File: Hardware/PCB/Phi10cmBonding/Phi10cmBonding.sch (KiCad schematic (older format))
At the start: 2 parts

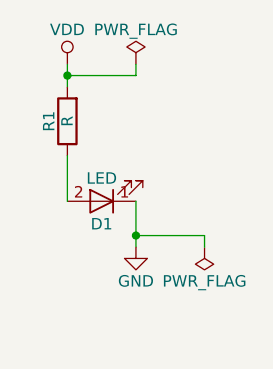
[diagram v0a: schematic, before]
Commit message: First example of correct net handling and zone filling
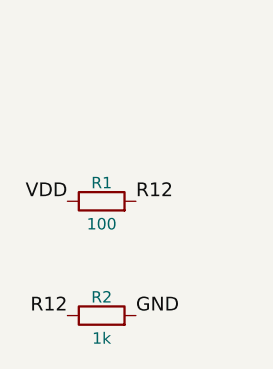
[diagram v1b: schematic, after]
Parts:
- removed D1: LED, LEDs:LED_0603, symbol LED
- added R2: 1k, Resistors_SMD:R_0603_HandSoldering, symbol R
- R1: value R -> 100
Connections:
- net GND: now also R2.2
- net VDD: now also R1.1; no longer R1.2
- new net R12: R1.2, R2.1
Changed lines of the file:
@@
 encoding utf-8
 Sheet 1 1
-Title "Topmetal-S sensor tiled plane, 10cm diameter version"
-Date "2017-03-28"
+Title "Python generated schematic with two resistors"
+Date ""
 Rev "0"
-Comp "LBNL"
+Comp "KiSch"
 Comment1 ""
 Comment2 ""
@@
 $EndDescr
 $Comp
-L LED D1
-U 1 1 58DA1C98
+L R R1
+U 1 1 58E4B144
 P 8000 5000
-F 0 "D1" H 8000 5100 50  0000 C CNN
-F 1 "LED" H 8000 4900 50  0000 C CNN
-F 2 "LEDs:LED_0603" H 8000 5000 50  0001 C CNN
+F 0 "R1" V 8080 5000 50  0000 C CNN
+F 1 "100" V 7900 5000 50  0000 C CNN
+F 2 "Resistors_SMD:R_0603_HandSoldering" V 7930 5000 50  0001 C CNN
 F 3 "" H 8000 5000 50  0001 C CNN
-	1    8000 5000
-	-1   0    0    1
+        1    8000 5000
+        0    -1   -1   0
 $EndComp
 $Comp
-L GND #PWR01
-U 1 1 58DA1D97
-P 8150 5200
-F 0 "#PWR01" H 8150 4950 50  0001 C CNN
-F 1 "GND" H 8150 5050 50  0000 C CNN
-F 2 "" H 8150 5200 50  0001 C CNN
-F 3 "" H 8150 5200 50  0001 C CNN
-	1    8150 5200
-	1    0    0    -1
+L R R2
+U 1 1 58E4B145
+P 8000 5500
+F 0 "R2" V 8080 5500 50  0000 C CNN
+F 1 "1k" V 7900 5500 50  0000 C CNN
+F 2 "Resistors_SMD:R_0603_HandSoldering" V 7930 5500 50  0001 C CNN
+F 3 "" H 8000 5500 50  0001 C CNN
+        1    8000 5500
+        0    -1   -1   0
 $EndComp
-$Comp
-L R R1
-U 1 1 58DA1DBE
-P 7850 4650
-F 0 "R1" V 7930 4650 50  0000 C CNN
-F 1 "R" V 7850 4650 50  0000 C CNN
-F 2 "Resistors_SMD:R_0603_HandSoldering" V 7780 4650 50  0001 C CNN
-F 3 "" H 7850 4650 50  0001 C CNN
-	1    7850 4650
-	-1   0    0    1
-$EndComp
-$Comp
-L VDD #PWR02
-U 1 1 58DA1E23
-P 7850 4400
-F 0 "#PWR02" H 7850 4250 50  0001 C CNN
-F 1 "VDD" H 7850 4550 50  0000 C CNN
-F 2 "" H 7850 4400 50  0001 C CNN
-F 3 "" H 7850 4400 50  0001 C CNN
-	1    7850 4400
-	1    0    0    -1
-$EndComp
-Wire Wire Line
-	7850 4400 7850 4500
-Wire Wire Line
-	7850 4800 7850 5000
-Wire Wire Line
-	8150 5000 8150 5200
-$Comp
-L PWR_FLAG #FLG03
-U 1 1 58DA1F76
-P 8150 4400
-F 0 "#FLG03" H 8150 4475 50  0001 C CNN
-F 1 "PWR_FLAG" H 8150 4550 50  0000 C CNN
-F 2 "" H 8150 4400 50  0001 C CNN
-F 3 "" H 8150 4400 50  0001 C CNN
-	1    8150 4400
-	1    0    0    -1
-$EndComp
-Wire Wire Line
-	8150 4400 8150 4450
-Wire Wire Line
-	8150 4450 7850 4450
-Connection ~ 7850 4450
-$Comp
-L PWR_FLAG #FLG04
-U 1 1 58DA1FB4
-P 8450 5200
-F 0 "#FLG04" H 8450 5275 50  0001 C CNN
-F 1 "PWR_FLAG" H 8450 5350 50  0000 C CNN
-F 2 "" H 8450 5200 50  0001 C CNN
-F 3 "" H 8450 5200 50  0001 C CNN
-	1    8450 5200
-	-1   0    0    1
-$EndComp
-Wire Wire Line
-	8450 5200 8450 5150
-Wire Wire Line
-	8450 5150 8150 5150
-Connection ~ 8150 5150
+Text Label 7850 5000 2    60   ~ 0
+VDD
+Text Label 8150 5000 0    60   ~ 0
+R12
+Text Label 7850 5500 2    60   ~ 0
+R12
+Text Label 8150 5500 0    60   ~ 0
+GND
 $EndSCHEMATC

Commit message: Add Topmetal-S schematic symbol lib and KiSch class to add it.
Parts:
- added U1: TMS1mm, symbol TMS1mm
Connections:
- net labels added: a1, a10, a11, a12, a13, a14, a15, a16, a17, a18, a19, a2, a20, a21, a22, a23, a24, a25, a26, a27, a28, a29, a3, a30, a31, a32, a33, a34, a35, a36, a37, a38, a39, a4, a40, a41, a42, a43, a44, a45, a46, a47, a48, a49, a5, a50, a6, a7, a8, a9
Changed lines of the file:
@@
 LIBS:contrib
 LIBS:valves
-EELAYER 25 0
+LIBS:TMSch
+EELAYER 26 0
 EELAYER END
 $Descr USLedger 17000 11000
@@
 $Comp
 L R R1
-U 1 1 58E4B144
+U 1 1 58EB4F46
 P 8000 5000
 F 0 "R1" V 8080 5000 50  0000 C CNN
@@
 F 2 "Resistors_SMD:R_0603_HandSoldering" V 7930 5000 50  0001 C CNN
 F 3 "" H 8000 5000 50  0001 C CNN
-        1    8000 5000
-        0    -1   -1   0
+       1    8000 5000
+       0    -1   -1   0
 $EndComp
 $Comp
 L R R2
-U 1 1 58E4B145
+U 1 1 58EB4F47
 P 8000 5500
 F 0 "R2" V 8080 5500 50  0000 C CNN
@@
 F 2 "Resistors_SMD:R_0603_HandSoldering" V 7930 5500 50  0001 C CNN
 F 3 "" H 8000 5500 50  0001 C CNN
-        1    8000 5500
-        0    -1   -1   0
+       1    8000 5500
+       0    -1   -1   0
 $EndComp
 Text Label 7850 5000 2    60   ~ 0
@@
 Text Label 8150 5500 0    60   ~ 0
 GND
+$Comp
+L TMS1mm U1
+U 0 1 58EB4F46
+P 4650 4350
+F 0 "U1" H 4600 5750 60  0000 C CNN
+F 1 "TMS1mm" H 4650 3050 60  0000 C CNN
+F 2 "" H 4580 4350 50  0000 C CNN
+F 3 "" H 4650 4350 50  0000 C CNN
+       0    4650 4350
+       1    0    0    -1
+$EndComp
+Text Label 3800 3200 2    60   ~ 0
+a1
+Text Label 3800 3300 2    60   ~ 0
+a2
+Text Label 3800 3400 2    60   ~ 0
+a3
+Text Label 3800 3500 2    60   ~ 0
+a4
+Text Label 3800 3600 2    60   ~ 0
+a5
+Text Label 3800 3700 2    60   ~ 0
+a6
+Text Label 3800 3800 2    60   ~ 0
+a7
+Text Label 3800 3900 2    60   ~ 0
+a8
+Text Label 3800 4000 2    60   ~ 0
+a9
+Text Label 3800 4100 2    60   ~ 0
+a10
+Text Label 3800 4200 2    60   ~ 0
+a11
+Text Label 3800 4300 2    60   ~ 0
+a12
+Text Label 3800 4400 2    60   ~ 0
+a13
+Text Label 3800 4500 2    60   ~ 0
+a14
+Text Label 3800 4600 2    60   ~ 0
+a15
+Text Label 3800 4700 2    60   ~ 0
+a16
+Text Label 3800 4800 2    60   ~ 0
+a17
+Text Label 3800 4900 2    60   ~ 0
+a18
+Text Label 3800 5000 2    60   ~ 0
+a19
+Text Label 3800 5100 2    60   ~ 0
+a20
+Text Label 3800 5200 2    60   ~ 0
+a21
+Text Label 3800 5300 2    60   ~ 0
+a22
+Text Label 3800 5400 2    60   ~ 0
+a23
+Text Label 3800 5500 2    60   ~ 0
+a24
+Text Label 5500 5600 0    60   ~ 0
+a25
+Text Label 5500 5500 0    60   ~ 0
+a26
+Text Label 5500 5400 0    60   ~ 0
+a27
+Text Label 5500 5300 0    60   ~ 0
+a28
+Text Label 5500 5200 0    60   ~ 0
+a29
+Text Label 5500 5100 0    60   ~ 0
+a30
+Text Label 5500 5000 0    60   ~ 0
+a31
+Text Label 5500 4900 0    60   ~ 0
+a32
+Text Label 5500 4800 0    60   ~ 0
+a33
+Text Label 5500 4700 0    60   ~ 0
+a34
+Text Label 5500 4600 0    60   ~ 0
+a35
+Text Label 5500 4500 0    60   ~ 0
+a36
+Text Label 5500 4400 0    60   ~ 0
+a37
+Text Label 5500 4300 0    60   ~ 0
+a38
+Text Label 5500 4200 0    60   ~ 0
+a39
+Text Label 5500 4100 0    60   ~ 0
+a40
+Text Label 5500 4000 0    60   ~ 0
+a41
+Text Label 5500 3900 0    60   ~ 0
+a42
+Text Label 5500 3800 0    60   ~ 0
+a43
+Text Label 5500 3700 0    60   ~ 0
+a44
+Text Label 5500 3600 0    60   ~ 0
+a45
+Text Label 5500 3500 0    60   ~ 0
+a46
+Text Label 5500 3400 0    60   ~ 0
+a47
+Text Label 5500 3300 0    60   ~ 0
+a48
+Text Label 5500 3200 0    60   ~ 0
+a49
+Text Label 5500 3100 0    60   ~ 0
+a50
 $EndSCHEMATC

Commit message: Add KiPcbFp footprint generation
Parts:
- removed U1: TMS1mm, symbol TMS1mm
- added U1: TMS1mm, Topmetal:TMS1mm, symbol TMS1mm
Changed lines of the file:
@@
 $Comp
 L R R1
-U 1 1 58EB4F46
+U 1 1 58ECDA2A
 P 8000 5000
 F 0 "R1" V 8080 5000 50  0000 C CNN
@@
 $Comp
 L R R2
-U 1 1 58EB4F47
+U 1 1 58ECDA2B
 P 8000 5500
 F 0 "R2" V 8080 5500 50  0000 C CNN
@@
 $Comp
 L TMS1mm U1
-U 0 1 58EB4F46
+U 1 1 58ECDA2C
 P 4650 4350
 F 0 "U1" H 4600 5750 60  0000 C CNN
 F 1 "TMS1mm" H 4650 3050 60  0000 C CNN
-F 2 "" H 4580 4350 50  0000 C CNN
+F 2 "Topmetal:TMS1mm" H 4580 4350 50  0000 C CNN
 F 3 "" H 4650 4350 50  0000 C CNN
        0    4650 4350

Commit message: Achieve reasonable array generation.
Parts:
- removed R1: 100, Resistors_SMD:R_0603_HandSoldering, symbol R
- removed R2: 1k, Resistors_SMD:R_0603_HandSoldering, symbol R
- added U0, U10, U100, U101, U102, U103, U104, U105, U106, U107, U108, U109, U11, U110, U111, U112, U113, U114, U115, U116, U117, U118, U119, U12, U120, U121, U122, U123, U124, U125, U126, U13, U14, U15, U16, U17, U18, U19, U2, U20, U21, U22, U23, U24, U25, U26, U27, U28, U29, U3, U30, U31, U32, U33, U34, U35, U36, U37, U38, U39, U4, U40, U41, U42, U43, U44, U45, U46, U47, U48, U49, U5, U50, U51, U52, U53, U54, U55, U56, U57, U58, U59, U6, U60, U61, U62, U63, U64, U65, U66, U67, U68, U69, U7, U70, U71, U72, U73, U74, U75, U76, U77, U78, U79, U8, U80, U81, U82, U83, U84, U85, U86, U87, U88, U89, U9, U90, U91, U92, U93, U94, U95, U96, U97, U98, U99: TMS1mm, Topmetal:TMS1mm, symbol TMS1mm
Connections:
- net labels added: AGND, AVDD, CLK_-1_N, CLK_-1_P, CLK_-2_N, CLK_-2_P, CLK_-3_N, CLK_-3_P, CLK_-4_N, CLK_-4_P, CLK_-5_N, CLK_-5_P, CLK_-6_N, CLK_-6_P, CLK_0_N, CLK_0_P, CLK_1_N, CLK_1_P, CLK_2_N, CLK_2_P, CLK_3_N, CLK_3_P, CLK_4_N, CLK_4_P, CLK_5_N, CLK_5_P, CLK_6_N, CLK_6_P, CSA_VBIASN_0, CSA_VBIASN_1, CSA_VBIASN_10, CSA_VBIASN_100, CSA_VBIASN_101, CSA_VBIASN_102, CSA_VBIASN_103, CSA_VBIASN_104, CSA_VBIASN_105, CSA_VBIASN_106, CSA_VBIASN_107, CSA_VBIASN_108, CSA_VBIASN_109, CSA_VBIASN_11, CSA_VBIASN_110, CSA_VBIASN_111, CSA_VBIASN_112, CSA_VBIASN_113, CSA_VBIASN_114, CSA_VBIASN_115, CSA_VBIASN_116, CSA_VBIASN_117, CSA_VBIASN_118, CSA_VBIASN_119, CSA_VBIASN_12, CSA_VBIASN_120, CSA_VBIASN_121, CSA_VBIASN_122, CSA_VBIASN_123, CSA_VBIASN_124, CSA_VBIASN_125, CSA_VBIASN_126, CSA_VBIASN_13, CSA_VBIASN_14, CSA_VBIASN_15, CSA_VBIASN_16, CSA_VBIASN_17, CSA_VBIASN_18, CSA_VBIASN_19, CSA_VBIASN_2, CSA_VBIASN_20, CSA_VBIASN_21, CSA_VBIASN_22, CSA_VBIASN_23, CSA_VBIASN_24, CSA_VBIASN_25, CSA_VBIASN_26, CSA_VBIASN_27, CSA_VBIASN_28, CSA_VBIASN_29, CSA_VBIASN_3, CSA_VBIASN_30, CSA_VBIASN_31, CSA_VBIASN_32, CSA_VBIASN_33, CSA_VBIASN_34, CSA_VBIASN_35, CSA_VBIASN_36, CSA_VBIASN_37, CSA_VBIASN_38, CSA_VBIASN_39, CSA_VBIASN_4, CSA_VBIASN_40, CSA_VBIASN_41, CSA_VBIASN_42, CSA_VBIASN_43, CSA_VBIASN_44, CSA_VBIASN_45, CSA_VBIASN_46, CSA_VBIASN_47, CSA_VBIASN_48, CSA_VBIASN_49, CSA_VBIASN_5, CSA_VBIASN_50, CSA_VBIASN_51, CSA_VBIASN_52, CSA_VBIASN_53, CSA_VBIASN_54, CSA_VBIASN_55, CSA_VBIASN_56, CSA_VBIASN_57, CSA_VBIASN_58, CSA_VBIASN_59, CSA_VBIASN_6, CSA_VBIASN_60, CSA_VBIASN_61, CSA_VBIASN_62, CSA_VBIASN_63, CSA_VBIASN_64, CSA_VBIASN_65, CSA_VBIASN_66, CSA_VBIASN_67, CSA_VBIASN_68, CSA_VBIASN_69, CSA_VBIASN_7, CSA_VBIASN_70, CSA_VBIASN_71, CSA_VBIASN_72, CSA_VBIASN_73, CSA_VBIASN_74, CSA_VBIASN_75, CSA_VBIASN_76, CSA_VBIASN_77, CSA_VBIASN_78, CSA_VBIASN_79, CSA_VBIASN_8, CSA_VBIASN_80, CSA_VBIASN_81, CSA_VBIASN_82, CSA_VBIASN_83, CSA_VBIASN_84, CSA_VBIASN_85, CSA_VBIASN_86, CSA_VBIASN_87, CSA_VBIASN_88, CSA_VBIASN_89, CSA_VBIASN_9, CSA_VBIASN_90, CSA_VBIASN_91, CSA_VBIASN_92, CSA_VBIASN_93, CSA_VBIASN_94, CSA_VBIASN_95, CSA_VBIASN_96, CSA_VBIASN_97, CSA_VBIASN_98, CSA_VBIASN_99, CSA_VBIASP_0, CSA_VBIASP_1, CSA_VBIASP_10, CSA_VBIASP_100, CSA_VBIASP_101, CSA_VBIASP_102, CSA_VBIASP_103, CSA_VBIASP_104, CSA_VBIASP_105, CSA_VBIASP_106, CSA_VBIASP_107, CSA_VBIASP_108, CSA_VBIASP_109, CSA_VBIASP_11, CSA_VBIASP_110, CSA_VBIASP_111, CSA_VBIASP_112, CSA_VBIASP_113, CSA_VBIASP_114, CSA_VBIASP_115, CSA_VBIASP_116, CSA_VBIASP_117, CSA_VBIASP_118, CSA_VBIASP_119, CSA_VBIASP_12, CSA_VBIASP_120, CSA_VBIASP_121, CSA_VBIASP_122, CSA_VBIASP_123, CSA_VBIASP_124, CSA_VBIASP_125, CSA_VBIASP_126, CSA_VBIASP_13, CSA_VBIASP_14, CSA_VBIASP_15, CSA_VBIASP_16, CSA_VBIASP_17, CSA_VBIASP_18, CSA_VBIASP_19, CSA_VBIASP_2, CSA_VBIASP_20, CSA_VBIASP_21, CSA_VBIASP_22, CSA_VBIASP_23, CSA_VBIASP_24, CSA_VBIASP_25, CSA_VBIASP_26, CSA_VBIASP_27, CSA_VBIASP_28, CSA_VBIASP_29, CSA_VBIASP_3, CSA_VBIASP_30, CSA_VBIASP_31, CSA_VBIASP_32, CSA_VBIASP_33, CSA_VBIASP_34, CSA_VBIASP_35, CSA_VBIASP_36, CSA_VBIASP_37, CSA_VBIASP_38, CSA_VBIASP_39, CSA_VBIASP_4, CSA_VBIASP_40, CSA_VBIASP_41, CSA_VBIASP_42, CSA_VBIASP_43, CSA_VBIASP_44, CSA_VBIASP_45, CSA_VBIASP_46, CSA_VBIASP_47, CSA_VBIASP_48, CSA_VBIASP_49, CSA_VBIASP_5, CSA_VBIASP_50, CSA_VBIASP_51, CSA_VBIASP_52, CSA_VBIASP_53, CSA_VBIASP_54, CSA_VBIASP_55, CSA_VBIASP_56, CSA_VBIASP_57, CSA_VBIASP_58, CSA_VBIASP_59, CSA_VBIASP_6, CSA_VBIASP_60, CSA_VBIASP_61, CSA_VBIASP_62, CSA_VBIASP_63, CSA_VBIASP_64, CSA_VBIASP_65, CSA_VBIASP_66, CSA_VBIASP_67, CSA_VBIASP_68, CSA_VBIASP_69, CSA_VBIASP_7, CSA_VBIASP_70, CSA_VBIASP_71, CSA_VBIASP_72, CSA_VBIASP_73, CSA_VBIASP_74, CSA_VBIASP_75, CSA_VBIASP_76, CSA_VBIASP_77, CSA_VBIASP_78, CSA_VBIASP_79, CSA_VBIASP_8, CSA_VBIASP_80, CSA_VBIASP_81, CSA_VBIASP_82, CSA_VBIASP_83, CSA_VBIASP_84, CSA_VBIASP_85, CSA_VBIASP_86, CSA_VBIASP_87, CSA_VBIASP_88, CSA_VBIASP_89, CSA_VBIASP_9, CSA_VBIASP_90, CSA_VBIASP_91, CSA_VBIASP_92, CSA_VBIASP_93, CSA_VBIASP_94, CSA_VBIASP_95, CSA_VBIASP_96, CSA_VBIASP_97, CSA_VBIASP_98, CSA_VBIASP_99, CSA_VDIS_0, CSA_VDIS_1, CSA_VDIS_10, CSA_VDIS_100, CSA_VDIS_101, CSA_VDIS_102, CSA_VDIS_103, CSA_VDIS_104, CSA_VDIS_105, CSA_VDIS_106, CSA_VDIS_107, CSA_VDIS_108, CSA_VDIS_109, CSA_VDIS_11, CSA_VDIS_110, CSA_VDIS_111, CSA_VDIS_112, CSA_VDIS_113, CSA_VDIS_114, CSA_VDIS_115, CSA_VDIS_116, CSA_VDIS_117, CSA_VDIS_118, CSA_VDIS_119, CSA_VDIS_12, CSA_VDIS_120, CSA_VDIS_121, CSA_VDIS_122, CSA_VDIS_123, CSA_VDIS_124, CSA_VDIS_125, CSA_VDIS_126, CSA_VDIS_13, CSA_VDIS_14, CSA_VDIS_15, CSA_VDIS_16, CSA_VDIS_17, CSA_VDIS_18, CSA_VDIS_19, CSA_VDIS_2, CSA_VDIS_20, CSA_VDIS_21, CSA_VDIS_22, CSA_VDIS_23, CSA_VDIS_24, CSA_VDIS_25, CSA_VDIS_26, CSA_VDIS_27, CSA_VDIS_28, CSA_VDIS_29, CSA_VDIS_3, CSA_VDIS_30, CSA_VDIS_31, CSA_VDIS_32, CSA_VDIS_33, CSA_VDIS_34, CSA_VDIS_35, CSA_VDIS_36, CSA_VDIS_37, CSA_VDIS_38, CSA_VDIS_39, CSA_VDIS_4, CSA_VDIS_40, CSA_VDIS_41, CSA_VDIS_42, CSA_VDIS_43, CSA_VDIS_44, CSA_VDIS_45, CSA_VDIS_46, CSA_VDIS_47, CSA_VDIS_48, CSA_VDIS_49, CSA_VDIS_5, CSA_VDIS_50, CSA_VDIS_51, CSA_VDIS_52, CSA_VDIS_53, CSA_VDIS_54, CSA_VDIS_55, CSA_VDIS_56, CSA_VDIS_57, CSA_VDIS_58, CSA_VDIS_59, CSA_VDIS_6, CSA_VDIS_60, CSA_VDIS_61, CSA_VDIS_62, CSA_VDIS_63, CSA_VDIS_64, CSA_VDIS_65, CSA_VDIS_66, CSA_VDIS_67, CSA_VDIS_68, CSA_VDIS_69, CSA_VDIS_7, CSA_VDIS_70, CSA_VDIS_71, CSA_VDIS_72, CSA_VDIS_73, CSA_VDIS_74, CSA_VDIS_75, CSA_VDIS_76, CSA_VDIS_77, CSA_VDIS_78, CSA_VDIS_79, CSA_VDIS_8, CSA_VDIS_80, CSA_VDIS_81, CSA_VDIS_82, CSA_VDIS_83, CSA_VDIS_84, CSA_VDIS_85, CSA_VDIS_86, CSA_VDIS_87, CSA_VDIS_88, CSA_VDIS_89, CSA_VDIS_9, CSA_VDIS_90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
- net labels removed: GND, R12, VDD, a1, a10, a11, a12, a13, a14, a15, a16, a17, a18, a19, a2, a20, a21, a22, a23, a24, a25, a26, a27, a28, a29, a3, a30, a31, a32, a33, a34, a35, a36, a37, a38, a39, a4, a40, a41, a42, a43, a44, a45, a46, a47, a48, a49, a5, a50, a6, a7, a8, a9
- no-connect marks 0 -> 762

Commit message: Add FSI-150-XX-X-D-X-XX connector symbol and footprint
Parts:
- removed U0, U1, U10, U100, U101, U102, U103, U104, U105, U106, U107, U108, U109, U11, U110, U111, U112, U113, U114, U115, U116, U117, U118, U119, U12, U120, U121, U122, U123, U124, U125, U126, U13, U14, U15, U16, U17, U18, U19, U2, U20, U21, U22, U23, U24, U25, U26, U27, U28, U29, U3, U30, U31, U32, U33, U34, U35, U36, U37, U38, U39, U4, U40, U41, U42, U43, U44, U45, U46, U47, U48, U49, U5, U50, U51, U52, U53, U54, U55, U56, U57, U58, U59, U6, U60, U61, U62, U63, U64, U65, U66, U67, U68, U69, U7, U70, U71, U72, U73, U74, U75, U76, U77, U78, U79, U8, U80, U81, U82, U83, U84, U85, U86, U87, U88, U89, U9, U90, U91, U92, U93, U94, U95, U96, U97, U98, U99: TMS1mm, Topmetal:TMS1mm, symbol TMS1mm
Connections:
- net labels removed: AGND, AVDD, CLK_-1_N, CLK_-1_P, CLK_-2_N, CLK_-2_P, CLK_-3_N, CLK_-3_P, CLK_-4_N, CLK_-4_P, CLK_-5_N, CLK_-5_P, CLK_-6_N, CLK_-6_P, CLK_0_N, CLK_0_P, CLK_1_N, CLK_1_P, CLK_2_N, CLK_2_P, CLK_3_N, CLK_3_P, CLK_4_N, CLK_4_P, CLK_5_N, CLK_5_P, CLK_6_N, CLK_6_P, CSA_VBIASN_0, CSA_VBIASN_1, CSA_VBIASN_10, CSA_VBIASN_100, CSA_VBIASN_101, CSA_VBIASN_102, CSA_VBIASN_103, CSA_VBIASN_104, CSA_VBIASN_105, CSA_VBIASN_106, CSA_VBIASN_107, CSA_VBIASN_108, CSA_VBIASN_109, CSA_VBIASN_11, CSA_VBIASN_110, CSA_VBIASN_111, CSA_VBIASN_112, CSA_VBIASN_113, CSA_VBIASN_114, CSA_VBIASN_115, CSA_VBIASN_116, CSA_VBIASN_117, CSA_VBIASN_118, CSA_VBIASN_119, CSA_VBIASN_12, CSA_VBIASN_120, CSA_VBIASN_121, CSA_VBIASN_122, CSA_VBIASN_123, CSA_VBIASN_124, CSA_VBIASN_125, CSA_VBIASN_126, CSA_VBIASN_13, CSA_VBIASN_14, CSA_VBIASN_15, CSA_VBIASN_16, CSA_VBIASN_17, CSA_VBIASN_18, CSA_VBIASN_19, CSA_VBIASN_2, CSA_VBIASN_20, CSA_VBIASN_21, CSA_VBIASN_22, CSA_VBIASN_23, CSA_VBIASN_24, CSA_VBIASN_25, CSA_VBIASN_26, CSA_VBIASN_27, CSA_VBIASN_28, CSA_VBIASN_29, CSA_VBIASN_3, CSA_VBIASN_30, CSA_VBIASN_31, CSA_VBIASN_32, CSA_VBIASN_33, CSA_VBIASN_34, CSA_VBIASN_35, CSA_VBIASN_36, CSA_VBIASN_37, CSA_VBIASN_38, CSA_VBIASN_39, CSA_VBIASN_4, CSA_VBIASN_40, CSA_VBIASN_41, CSA_VBIASN_42, CSA_VBIASN_43, CSA_VBIASN_44, CSA_VBIASN_45, CSA_VBIASN_46, CSA_VBIASN_47, CSA_VBIASN_48, CSA_VBIASN_49, CSA_VBIASN_5, CSA_VBIASN_50, CSA_VBIASN_51, CSA_VBIASN_52, CSA_VBIASN_53, CSA_VBIASN_54, CSA_VBIASN_55, CSA_VBIASN_56, CSA_VBIASN_57, CSA_VBIASN_58, CSA_VBIASN_59, CSA_VBIASN_6, CSA_VBIASN_60, CSA_VBIASN_61, CSA_VBIASN_62, CSA_VBIASN_63, CSA_VBIASN_64, CSA_VBIASN_65, CSA_VBIASN_66, CSA_VBIASN_67, CSA_VBIASN_68, CSA_VBIASN_69, CSA_VBIASN_7, CSA_VBIASN_70, CSA_VBIASN_71, CSA_VBIASN_72, CSA_VBIASN_73, CSA_VBIASN_74, CSA_VBIASN_75, CSA_VBIASN_76, CSA_VBIASN_77, CSA_VBIASN_78, CSA_VBIASN_79, CSA_VBIASN_8, CSA_VBIASN_80, CSA_VBIASN_81, CSA_VBIASN_82, CSA_VBIASN_83, CSA_VBIASN_84, CSA_VBIASN_85, CSA_VBIASN_86, CSA_VBIASN_87, CSA_VBIASN_88, CSA_VBIASN_89, CSA_VBIASN_9, CSA_VBIASN_90, CSA_VBIASN_91, CSA_VBIASN_92, CSA_VBIASN_93, CSA_VBIASN_94, CSA_VBIASN_95, CSA_VBIASN_96, CSA_VBIASN_97, CSA_VBIASN_98, CSA_VBIASN_99, CSA_VBIASP_0, CSA_VBIASP_1, CSA_VBIASP_10, CSA_VBIASP_100, CSA_VBIASP_101, CSA_VBIASP_102, CSA_VBIASP_103, CSA_VBIASP_104, CSA_VBIASP_105, CSA_VBIASP_106, CSA_VBIASP_107, CSA_VBIASP_108, CSA_VBIASP_109, CSA_VBIASP_11, CSA_VBIASP_110, CSA_VBIASP_111, CSA_VBIASP_112, CSA_VBIASP_113, CSA_VBIASP_114, CSA_VBIASP_115, CSA_VBIASP_116, CSA_VBIASP_117, CSA_VBIASP_118, CSA_VBIASP_119, CSA_VBIASP_12, CSA_VBIASP_120, CSA_VBIASP_121, CSA_VBIASP_122, CSA_VBIASP_123, CSA_VBIASP_124, CSA_VBIASP_125, CSA_VBIASP_126, CSA_VBIASP_13, CSA_VBIASP_14, CSA_VBIASP_15, CSA_VBIASP_16, CSA_VBIASP_17, CSA_VBIASP_18, CSA_VBIASP_19, CSA_VBIASP_2, CSA_VBIASP_20, CSA_VBIASP_21, CSA_VBIASP_22, CSA_VBIASP_23, CSA_VBIASP_24, CSA_VBIASP_25, CSA_VBIASP_26, CSA_VBIASP_27, CSA_VBIASP_28, CSA_VBIASP_29, CSA_VBIASP_3, CSA_VBIASP_30, CSA_VBIASP_31, CSA_VBIASP_32, CSA_VBIASP_33, CSA_VBIASP_34, CSA_VBIASP_35, CSA_VBIASP_36, CSA_VBIASP_37, CSA_VBIASP_38, CSA_VBIASP_39, CSA_VBIASP_4, CSA_VBIASP_40, CSA_VBIASP_41, CSA_VBIASP_42, CSA_VBIASP_43, CSA_VBIASP_44, CSA_VBIASP_45, CSA_VBIASP_46, CSA_VBIASP_47, CSA_VBIASP_48, CSA_VBIASP_49, CSA_VBIASP_5, CSA_VBIASP_50, CSA_VBIASP_51, CSA_VBIASP_52, CSA_VBIASP_53, CSA_VBIASP_54, CSA_VBIASP_55, CSA_VBIASP_56, CSA_VBIASP_57, CSA_VBIASP_58, CSA_VBIASP_59, CSA_VBIASP_6, CSA_VBIASP_60, CSA_VBIASP_61, CSA_VBIASP_62, CSA_VBIASP_63, CSA_VBIASP_64, CSA_VBIASP_65, CSA_VBIASP_66, CSA_VBIASP_67, CSA_VBIASP_68, CSA_VBIASP_69, CSA_VBIASP_7, CSA_VBIASP_70, CSA_VBIASP_71, CSA_VBIASP_72, CSA_VBIASP_73, CSA_VBIASP_74, CSA_VBIASP_75, CSA_VBIASP_76, CSA_VBIASP_77, CSA_VBIASP_78, CSA_VBIASP_79, CSA_VBIASP_8, CSA_VBIASP_80, CSA_VBIASP_81, CSA_VBIASP_82, CSA_VBIASP_83, CSA_VBIASP_84, CSA_VBIASP_85, CSA_VBIASP_86, CSA_VBIASP_87, CSA_VBIASP_88, CSA_VBIASP_89, CSA_VBIASP_9, CSA_VBIASP_90, CSA_VBIASP_91, CSA_VBIASP_92, CSA_VBIASP_93, CSA_VBIASP_94, CSA_VBIASP_95, CSA_VBIASP_96, CSA_VBIASP_97, CSA_VBIASP_98, CSA_VBIASP_99, CSA_VDIS_0, CSA_VDIS_1, CSA_VDIS_10, CSA_VDIS_100, CSA_VDIS_101, CSA_VDIS_102, CSA_VDIS_103, CSA_VDIS_104, CSA_VDIS_105, CSA_VDIS_106, CSA_VDIS_107, CSA_VDIS_108, CSA_VDIS_109, CSA_VDIS_11, CSA_VDIS_110, CSA_VDIS_111, CSA_VDIS_112, CSA_VDIS_113, CSA_VDIS_114, CSA_VDIS_115, CSA_VDIS_116, CSA_VDIS_117, CSA_VDIS_118, CSA_VDIS_119, CSA_VDIS_12, CSA_VDIS_120, CSA_VDIS_121, CSA_VDIS_122, CSA_VDIS_123, CSA_VDIS_124, CSA_VDIS_125, CSA_VDIS_126, CSA_VDIS_13, CSA_VDIS_14, CSA_VDIS_15, CSA_VDIS_16, CSA_VDIS_17, CSA_VDIS_18, CSA_VDIS_19, CSA_VDIS_2, CSA_VDIS_20, CSA_VDIS_21, CSA_VDIS_22, CSA_VDIS_23, CSA_VDIS_24, CSA_VDIS_25, CSA_VDIS_26, CSA_VDIS_27, CSA_VDIS_28, CSA_VDIS_29, CSA_VDIS_3, CSA_VDIS_30, CSA_VDIS_31, CSA_VDIS_32, CSA_VDIS_33, CSA_VDIS_34, CSA_VDIS_35, CSA_VDIS_36, CSA_VDIS_37, CSA_VDIS_38, CSA_VDIS_39, CSA_VDIS_4, CSA_VDIS_40, CSA_VDIS_41, CSA_VDIS_42, CSA_VDIS_43, CSA_VDIS_44, CSA_VDIS_45, CSA_VDIS_46, CSA_VDIS_47, CSA_VDIS_48, CSA_VDIS_49, CSA_VDIS_5, CSA_VDIS_50, CSA_VDIS_51, CSA_VDIS_52, CSA_VDIS_53, CSA_VDIS_54, CSA_VDIS_55, CSA_VDIS_56, CSA_VDIS_57, CSA_VDIS_58, CSA_VDIS_59, CSA_VDIS_6, CSA_VDIS_60, CSA_VDIS_61, CSA_VDIS_62, CSA_VDIS_63, CSA_VDIS_64, CSA_VDIS_65, CSA_VDIS_66, CSA_VDIS_67, CSA_VDIS_68, CSA_VDIS_69, CSA_VDIS_7, CSA_VDIS_70, CSA_VDIS_71, CSA_VDIS_72, CSA_VDIS_73, CSA_VDIS_74, CSA_VDIS_75, CSA_VDIS_76, CSA_VDIS_77, CSA_VDIS_78, CSA_VDIS_79, CSA_VDIS_8, CSA_VDIS_80, CSA_VDIS_81, CSA_VDIS_82, CSA_VDIS_83, CSA_VDIS_84, CSA_VDIS_85, CSA_VDIS_86, CSA_VDIS_87, CSA_VDIS_88, CSA_VDIS_89, CSA_VDIS_9, CSA_VDIS_90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
- no-connect marks 762 -> 0
